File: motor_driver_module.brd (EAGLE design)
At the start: 160 x 100 mm, 55 parts, among them IC1 LTC6088, IC7 DRV8833RTY, IC8 DRV8833RTY, P1 BAT+, P10 MD2, P11 MA_IN1, P12 MA_IN2, P13 MB_IN1, P14 MB_IN2, P15 MC_IN1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

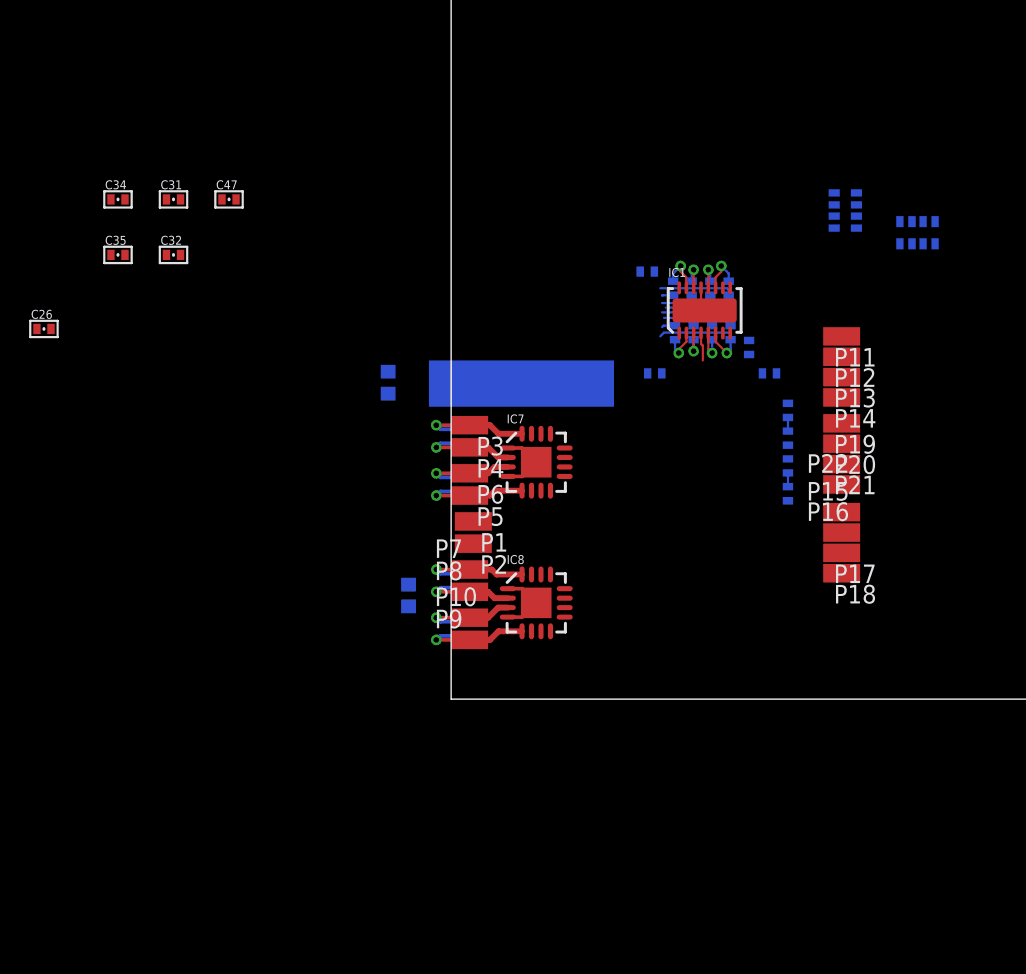
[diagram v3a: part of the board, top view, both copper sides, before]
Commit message: More routing. No progress.
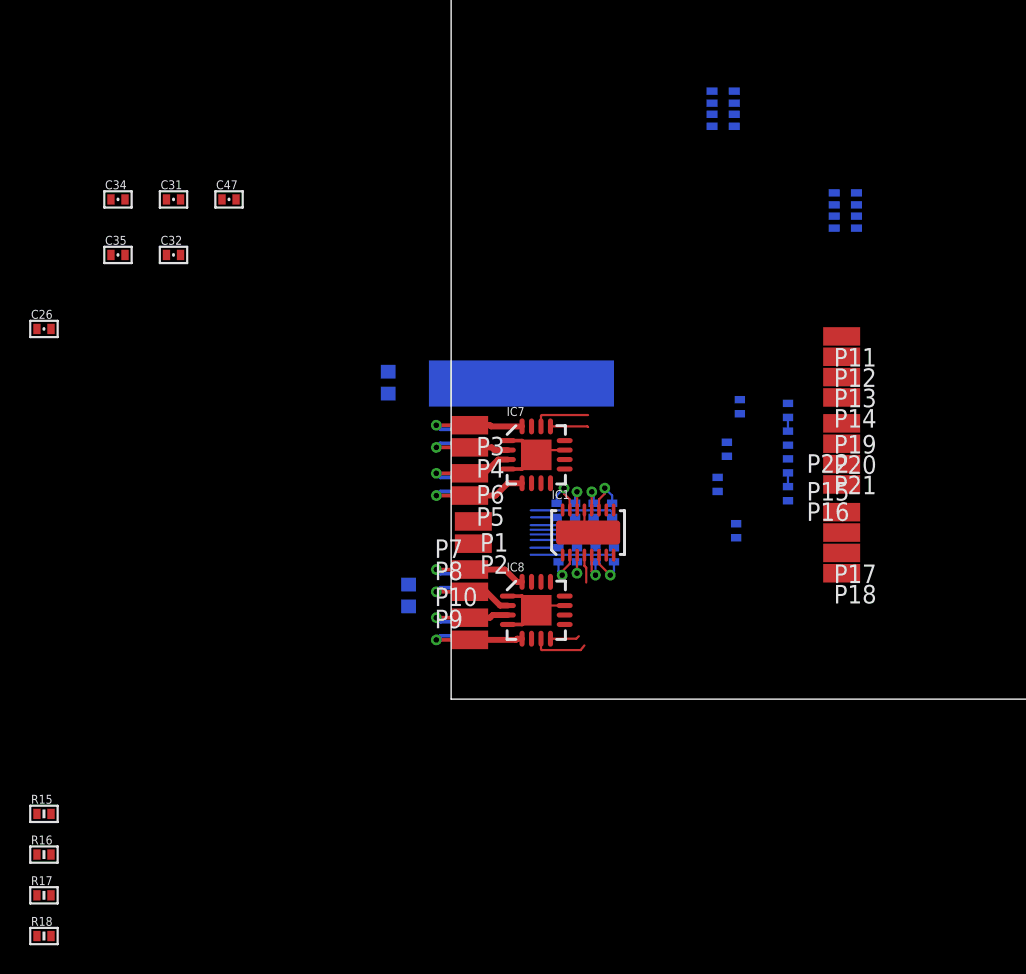
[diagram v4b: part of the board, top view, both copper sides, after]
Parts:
- added R15, R16, R17, R18: (no value), biomimetic:0402-RES
- moved IC1 17.2 mm to (9.40, 11.4)
- moved R2 17.2 mm to (8.64, 9.91)
- moved R4 17.2 mm to (7.37, 9.91)
- moved R10 17.2 mm to (9.78, 13.0)
- moved R11 17.2 mm to (11.0, 13.0)
- moved R5 17.2 mm to (8.51, 13.0)
- moved R6 17.2 mm to (7.24, 13.0)
- moved R7 17.2 mm to (9.91, 9.91)
- moved R9 17.2 mm to (11.2, 9.91)
- moved R1 15.8 mm to (18.7, 40.5), turned to 90 degrees
- moved R12 13.4 mm to (18.9, 17.1), turned to 270 degrees
- moved R14 11.0 mm to (19.6, 11.6), turned to 270 degrees
- moved R13 9.64 mm to (18.3, 14.7)
- moved R3 6.27 mm to (19.8, 20.1), turned to 90 degrees
- moved IC8 0.51 mm to (5.84, 6.10)
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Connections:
- net N$22: now also R16.1; no longer R8.1
- net N$24: now also R17.1; no longer R1.4
- net N$26: now also R18.1; no longer R1.1
- net N$30: now also R15.1; no longer R8.4
- net N$34: now also R18.2; no longer R1.8
- net N$35: now also R17.2; no longer R1.5
- net N$36: now also R15.2; no longer R8.5
- net N$37: now also R16.2; no longer R8.8
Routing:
- net GND: track 12.9 -> 17.1 mm
- net MOTOR_A_IN1: track 0.00 -> 3.98 mm
- net MOTOR_D_IN1: track 0.00 -> 3.88 mm
- net MOTOR_A_IN2: track 0.00 -> 2.60 mm
- net MOTOR_D_IN2: track 0.00 -> 2.02 mm
- net MOTOR_C_OUT1: track 11.6 -> 12.8 mm
- net MOTOR_B_OUT1: track 10.3 -> 11.5 mm
- net MOTOR_B_OUT2: track 7.63 -> 8.82 mm
- net MOTOR_D_OUT1: track 11.5 -> 12.6 mm
- net MOTOR_C_OUT2: track 11.9 -> 12.9 mm
- net MOTOR_A_OUT1: track 10.4 -> 11.3 mm
- net MOTOR_A_OUT2: track 7.89 -> 8.68 mm
- net MOTOR_D_OUT2: track 12.1 -> 12.7 mm

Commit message: Further routing. No progress.
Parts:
- added R19, R20: (no value), biomimetic:0402-RES
- R1, R8: value 15k -> (none); device OPL Eagle Library:R1206-8 -> biomimetic:0402-RES
- moved R15 54.2 mm to (23.6, 8.89)
- moved R16 54.2 mm to (23.6, 6.10)
- moved R17 54.2 mm to (23.6, 3.30)
- moved R18 54.2 mm to (23.6, 0.51)
- moved R1 43.1 mm to (23.6, -2.29), flipped to the top, turned to 0 degrees
- moved R8 38.8 mm to (23.6, -5.08), flipped to the top, turned to 0 degrees
- moved R10 13.4 mm to (3.94, 0.89), turned to 180 degrees
- moved R11 12.9 mm to (3.94, 2.16), turned to 180 degrees
- moved R9 9.42 mm to (3.68, 4.19), turned to 180 degrees
- moved R2 7.70 mm to (3.94, 16.0), turned to 180 degrees
- moved R7 7.65 mm to (3.68, 5.46), turned to 180 degrees
- moved R4 5.92 mm to (3.94, 14.7), turned to 180 degrees
- moved R5 4.78 mm to (3.94, 11.6), turned to 180 degrees
- moved C27 3.69 mm to (2.03, 4.83)
- moved P7 3.69 mm to (2.92, 5.59)
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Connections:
- net N$22: now also IC1.3; no longer IC1.14
- net N$23: now also IC1.2, R8.2; no longer IC1.15, R8.7
- net N$25: now also R19.2; no longer R1.6
- net N$27: now also R20.2; no longer R1.7
- net N$30: now also IC1.14; no longer IC1.3
- net N$31: now also IC1.15, R1.2; no longer IC1.2, R8.6
- net N$36: now also IC1.16; no longer IC1.1
- net N$37: now also IC1.1; no longer IC1.16
- net V_REF: now also R1.1, R19.1, R20.1, R8.1; no longer R1.2, R1.3, R8.2, R8.3
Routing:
- net V_BATT: track 0.00 -> 43.5 mm, vias 0 -> 5
- net MOTOR_C_OUT2: track 12.9 -> 6.81 mm
- net MOTOR_D_OUT2: track 12.7 -> 6.75 mm
- net MOTOR_C_OUT1: track 12.8 -> 7.75 mm
- net MOTOR_D_OUT1: track 12.6 -> 8.94 mm
- net MOTOR_A_OUT1: track 11.3 -> 7.68 mm
- net MOTOR_C_IN1: track 0.00 -> 3.44 mm
- net MOTOR_B_IN1: track 0.00 -> 3.25 mm
- net N$27: track 2.91 -> 0.00 mm, vias 1 -> 0
- net N$23: track 2.91 -> 0.00 mm, vias 1 -> 0
- net N$24: track 2.75 -> 0.00 mm, vias 1 -> 0
- net N$25: track 2.71 -> 0.00 mm, vias 1 -> 0
- net GND: track 17.1 -> 19.8 mm, vias 0 -> 4
- net N$31: track 2.61 -> 0.03 mm, vias 1 -> 0
- net N$22: track 2.09 -> 0.00 mm, vias 1 -> 0
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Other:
- board size 160 x 100 mm -> 34.7 x 17.1 mm
